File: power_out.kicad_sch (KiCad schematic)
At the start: 20 parts, among them Q501 BTN8962TA, Q502 BTN8962TA, U501 BTT6200-4ESA

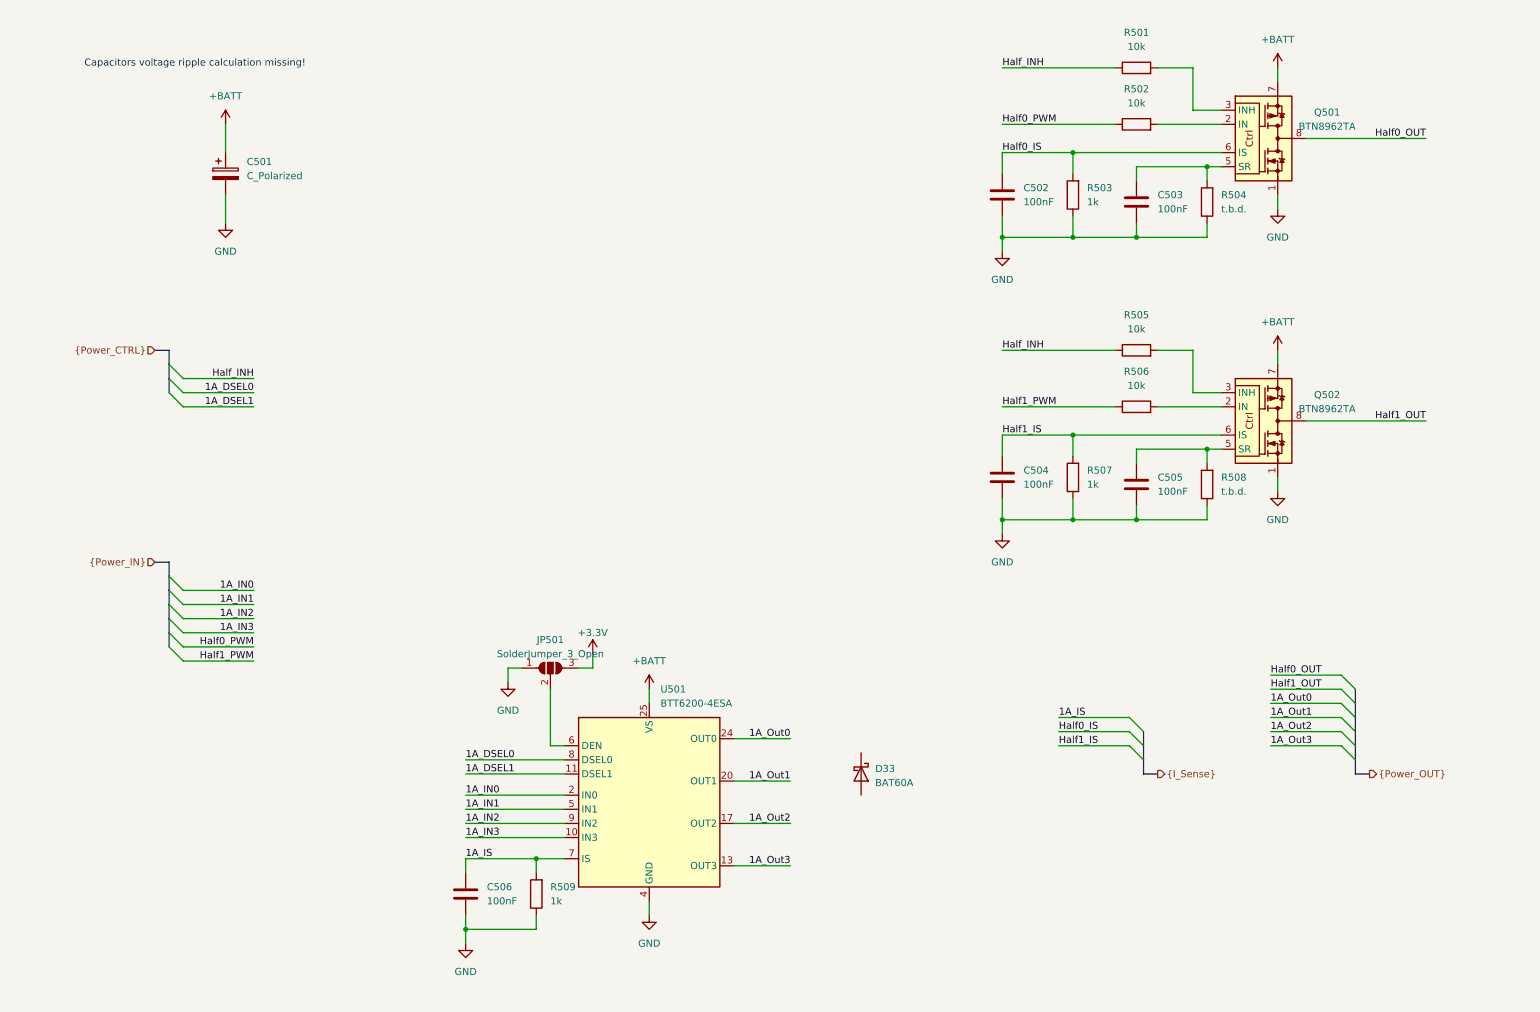
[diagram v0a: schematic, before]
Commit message: added net-classes
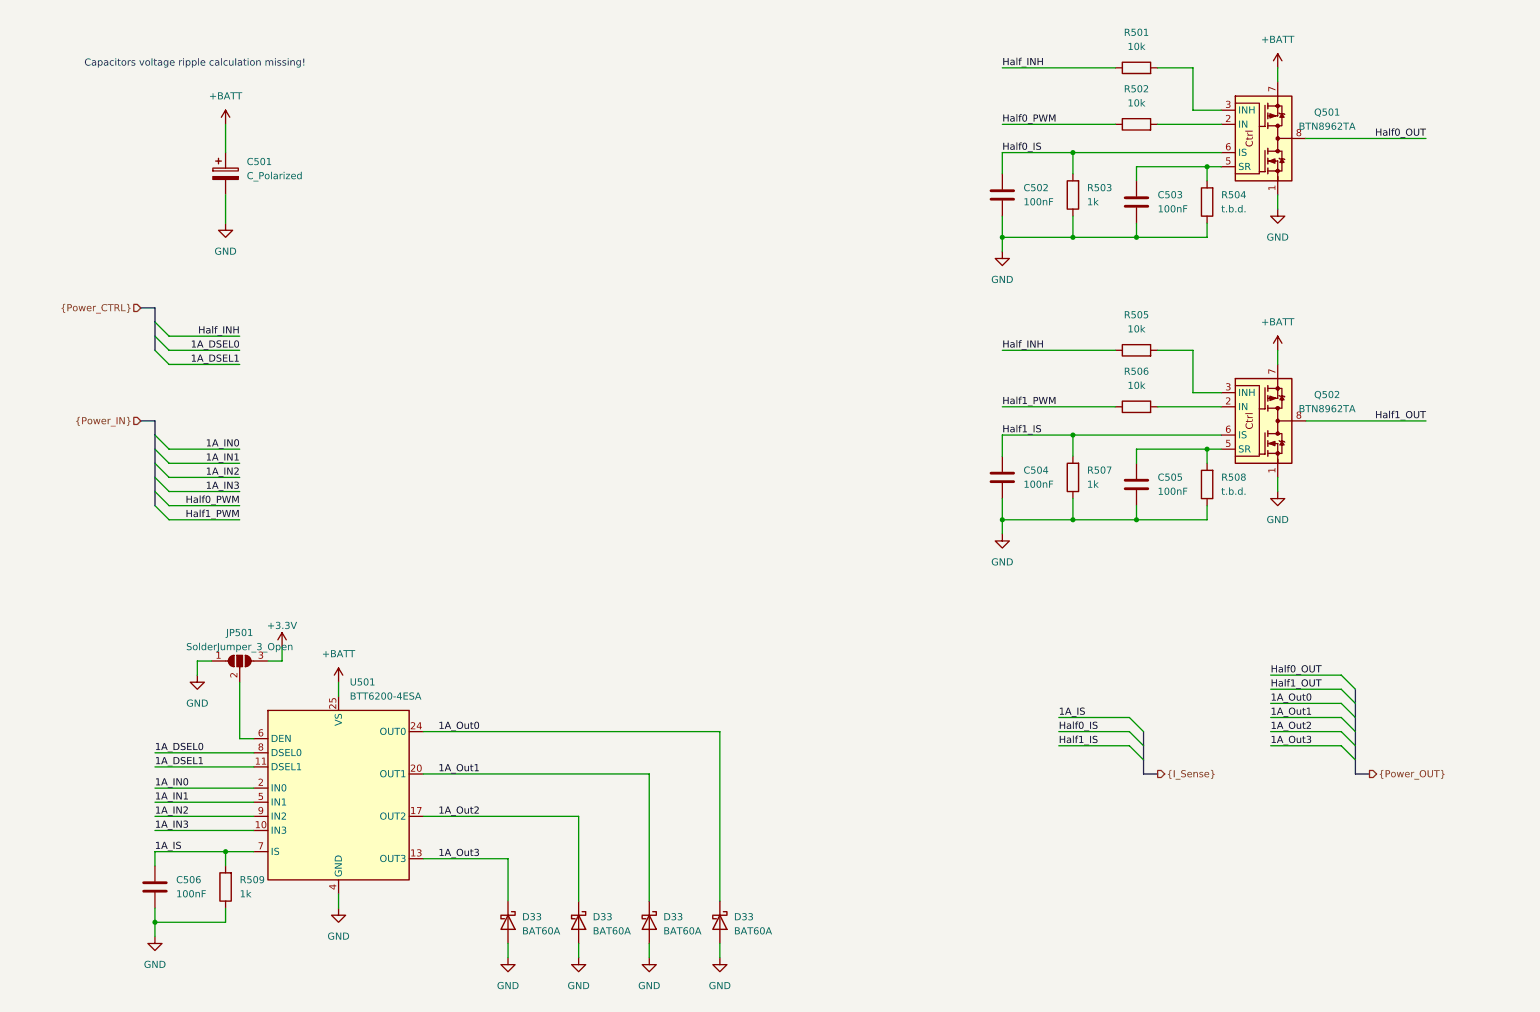
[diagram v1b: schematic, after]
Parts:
- added D33 (x3): BAT60A, Diode_SMD:D_SOD-323, symbol Diode:BAT60A
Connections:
- net 1A_Out0: now also D33.1 (K)
- net 1A_Out1: now also D33.1 (K)
- net 1A_Out2: now also D33.1 (K)
- net 1A_Out3: now also D33.1 (K)
- net GND: now also D33.2 (A), D33.2 (A), D33.2 (A), D33.2 (A)
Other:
- moved on the sheet: C506, D33, JP501, R509, U501

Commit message: completed schematic
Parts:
- removed D33 (x4): BAT60A, Diode_SMD:D_SOD-323, symbol Diode:BAT60A
- added C507: 220µ, symbol Device:C_Polarized
- added C508, C509, C510, C511, C512, C513, C518: 100nF, Capacitor_SMD:C_0603_1608Metric, symbol Device:C
- added C514, C515, C516, C517: 10n, Capacitor_SMD:C_0603_1608Metric, symbol Device:C
- added C519: 1µ, Capacitor_SMD:C_0603_1608Metric, symbol Device:C
- added D501, D502, D503, D504, D513: PMEG4010CEH, Diode_SMD:D_SOD-123F, symbol Diode:PMEG4010CEH
- added D506, D507, D508, D509, D510, D511: BLUE, LED_SMD:LED_0603_1608Metric, symbol Device:LED
- added D512: RED, LED_SMD:LED_0603_1608Metric, symbol Device:LED
- added R510, R511, R512, R513: 100k, Resistor_SMD:R_0603_1608Metric, symbol Device:R
- added R514, R515, R516, R517, R518, R519, R520, R522, R523, R524, R525, R526, R527: 10k, Resistor_SMD:R_0603_1608Metric, symbol Device:R
- added R521: 27, Resistor_SMD:R_0603_1608Metric, symbol Device:R
- added R528: 1k, Resistor_SMD:R_0603_1608Metric, symbol Device:R
- C501: value C_Polarized -> 220µ
- C502, C504: value 100nF -> 1n
- C506: value 100nF -> 100p
- R509: value 1k -> 1.2k
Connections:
- net +3.3V: now also R528.2
- net +BATT: now also C507.1, C509.1, C510.1, C511.1, C513.1, C518.1, C519.1
- net 1A_DSEL0: now also R514.1; no longer U501.8 (DSEL0)
- net 1A_DSEL1: now also R515.1; no longer U501.11 (DSEL1)
- net 1A_IN0: now also R516.1; no longer U501.2 (IN0)
- net 1A_IN1: now also R517.1; no longer U501.5 (IN1)
- net 1A_IN2: now also R518.1; no longer U501.9 (IN2)
- net 1A_IN3: now also R519.1; no longer U501.10 (IN3)
- net 1A_IS: now also R520.2; no longer R509.2, U501.7 (IS)
- net 1A_Out0: now also C517.1, D513.1 (K), R513.2, R524.2
- net 1A_Out1: now also C516.1, D504.1 (K), R512.2, R525.2
- net 1A_Out2: now also C515.1, D503.1 (K), R511.2, R526.2
- net 1A_Out3: now also C514.1, D502.1 (K), R510.2, R527.2
- net GND: now also C507.2, C508.2, C510.2, C512.2, C513.2, C514.2, C515.2, C516.2, C517.2, C518.2, C519.2, D501.1 (K), D502.2 (A), D503.2 (A), D504.2 (A), D506.1 (K), D507.1 (K), D508.1 (K), D509.1 (K), D510.1 (K), D511.1 (K), D513.2 (A), R510.1, R511.1, R512.1, R513.1; no longer U501.4 (GND)
- net Half0_OUT: now also C508.1, C509.2, R523.2
- net Half1_OUT: now also C511.2, C512.1, R522.2
- net Half_INH: now also D512.1 (K)
- new net: R519.2, U501.10 (IN3)
- new net: D508.2 (A), R524.1
- new net: D512.2 (A), R528.1
- new net: D507.2 (A), R522.1
- new net: R517.2, U501.5 (IN1)
- new net: D509.2 (A), R525.1
- new net: R509.2, R520.1, U501.7 (IS)
- new net: D511.2 (A), R527.1
- new net: D501.2 (A), R521.1
- new net: R521.2, U501.4 (GND)
- new net: R514.2, U501.8 (DSEL0)
- new net: D510.2 (A), R526.1
- new net: R516.2, U501.2 (IN0)
- new net: D506.2 (A), R523.1
- new net: R515.2, U501.11 (DSEL1)
- new net: R518.2, U501.9 (IN2)
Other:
- note removed: "Capacitors voltage ripple calculation missing!"
- moved on the sheet: C501, C502, C503, C504, C505, C506, JP501, Q501, Q502, R501, R502, R503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

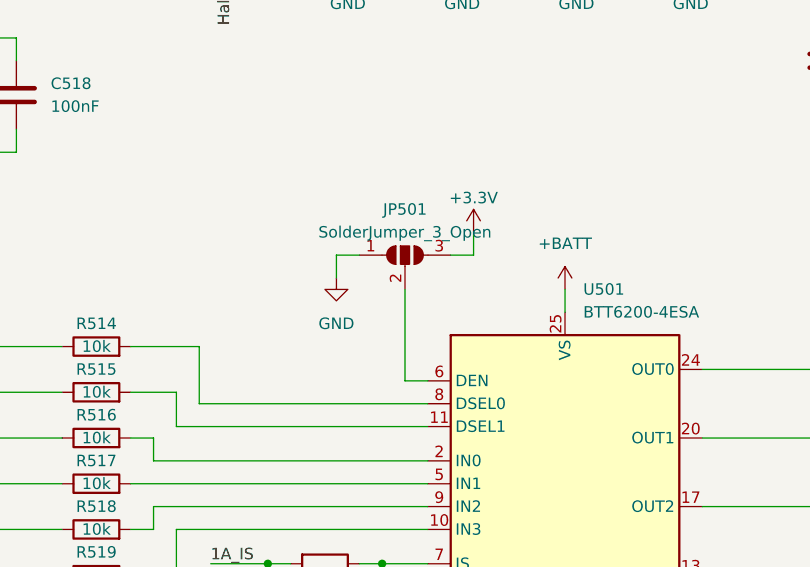
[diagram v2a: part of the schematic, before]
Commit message: placed components and began routing
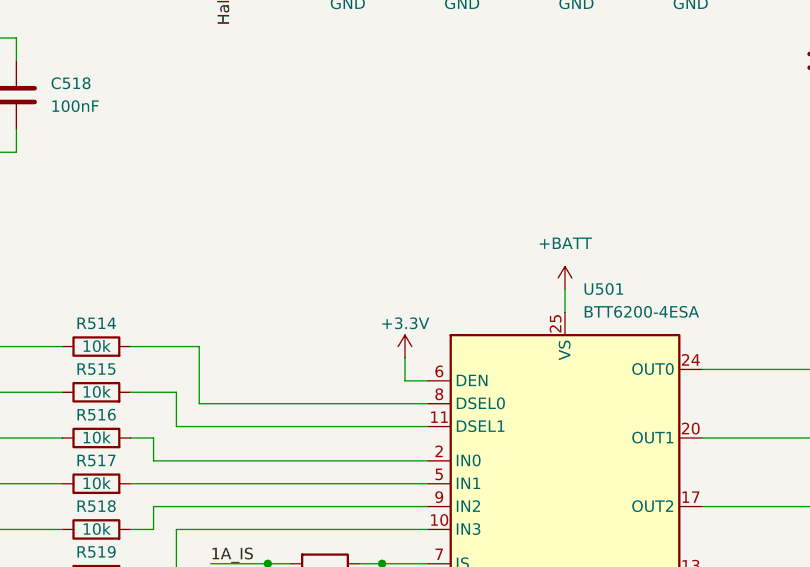
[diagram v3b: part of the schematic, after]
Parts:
- removed JP501: SolderJumper_3_Open, Jumper:SolderJumper-3_P1.3mm_Open_Pad1.0x1.5mm, symbol Jumper:SolderJumper_3_Open
- C501, C507: footprint (none) -> Capacitor_SMD:CP_Elec_10x10.5
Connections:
- net +3.3V: now also U501.6 (DEN)
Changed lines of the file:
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@@
-    (stroke (width 0) (type default))
-  )
-  (wire (pts (xy 74.93 119.38) (xy 72.39 119.38))
     (stroke (width 0) (type default))
   )
@@
     (stroke (width 0) (type default))
   )
-  (wire (pts (xy 87.63 119.38) (xy 87.63 116.84))
-    (stroke (width 0) (type default))
-  )
   (wire (pts (xy 25.4 139.7) (xy 41.91 139.7))
     (stroke (width 0) (type default))
@@
     (stroke (width 0) (type default))
   )
-  (wire (pts (xy 85.09 119.38) (xy 87.63 119.38))
-    (stroke (width 0) (type default))
-  )
   (wire (pts (xy 231.14 57.15) (xy 231.14 59.69))
     (stroke (width 0) (type default))
@@
     (stroke (width 0) (type default))
   )
+  (wire (pts (xy 80.01 130.81) (xy 80.01 133.35))
+    (stroke (width 0) (type default))
+  )
   (wire (pts (xy 190.5 36.83) (xy 231.14 36.83))
     (stroke (width 0) (type default))
@@
     (stroke (width 0) (type default))
   )
-  (wire (pts (xy 80.01 123.19) (xy 80.01 133.35))
-    (stroke (width 0) (type default))
-  )
   (wire (pts (xy 111.76 83.82) (xy 111.76 86.36))
     (stroke (width 0) (type default))
@@
   )
   (wire (pts (xy 113.03 154.94) (xy 118.11 154.94))
-    (stroke (width 0) (type default))
-  )
-  (wire (pts (xy 72.39 119.38) (xy 72.39 121.92))
     (stroke (width 0) (type default))
   )
@@
         (path "/e63e39d7-6ac0-4ffd-8aa3-1841a4541b55/39fda93f-20d1-454a-b043-914b0964bf2d"
           (reference "#PWR0120") (unit 1)
-        )
-      )
-    )
-  )
-  (symbol (lib_id "power:GND") (at 72.39 121.92 0) (unit 1)
-    (in_bom yes) (on_board yes) (dnp no) (fields_autoplaced)
-    (property "Reference" "#PWR0510" (at 72.39 128.27 0)
-      (effects (font (size 1.27 1.27)) hide)
-    )
-    (property "Value" "GND" (at 72.39 127 0)
-      (effects (font (size 1.27 1.27)))
-    )
-    (property "Footprint" "" (at 72.39 121.92 0)
-      (effects (font (size 1.27 1.27)) hide)
-    )
-    (property "Datasheet" "" (at 72.39 121.92 0)
-      (effects (font (size 1.27 1.27)) hide)
-    )
-    (pin "1")
-    (instances
-      (project "Sensor_Board"
-        (path "/e2a0eb17-0eae-4cdd-befd-118f8728b921/c1280e85-b203-4b6b-82d8-dbf0409d7c4d"
-          (reference "#PWR0510") (unit 1)
-        )
-      )
-      (project "FT22_VCU_Konzept"
-        (path "/e63e39d7-6ac0-4ffd-8aa3-1841a4541b55/39fda93f-20d1-454a-b043-914b0964bf2d"
-          (reference "#PWR0126") (unit 1)
         )
       )
@@
     )
   )
-  (symbol (lib_id "power:+3.3V") (at 87.63 116.84 0) (unit 1)
-    (in_bom yes) (on_board yes) (dnp no) (fields_autoplaced)
-    (property "Reference" "#PWR0509" (at 87.63 120.65 0)
-      (effects (font (size 1.27 1.27)) hide)
-    )
-    (property "Value" "+3.3V" (at 87.63 113.03 0)
-      (effects (font (size 1.27 1.27)))
-    )
-    (property "Footprint" "" (at 87.63 116.84 0)
-      (effects (font (size 1.27 1.27)) hide)
-    )
-    (property "Datasheet" "" (at 87.63 116.84 0)
+  (symbol (lib_id "power:+3.3V") (at 80.01 130.81 0) (unit 1)
+    (in_bom yes) (on_board yes) (dnp no) (fields_autoplaced)
+    (property "Reference" "#PWR0509" (at 80.01 134.62 0)
+      (effects (font (size 1.27 1.27)) hide)
+    )
+    (property "Value" "+3.3V" (at 80.01 127 0)
+      (effects (font (size 1.27 1.27)))
+    )
+    (property "Footprint" "" (at 80.01 130.81 0)
+      (effects (font (size 1.27 1.27)) hide)
+    )
+    (property "Datasheet" "" (at 80.01 130.81 0)
       (effects (font (size 1.27 1.27)) hide)
     )
@@
         (path "/e63e39d7-6ac0-4ffd-8aa3-1841a4541b55/39fda93f-20d1-454a-b043-914b0964bf2d"
           (reference "C50") (unit 1)
-        )
-      )
-    )
-  )
-  (symbol (lib_id "Jumper:SolderJumper_3_Open") (at 80.01 119.38 0) (unit 1)
-    (in_bom yes) (on_board yes) (dnp no) (fields_autoplaced)
-    (property "Reference" "JP501" (at 80.01 114.3 0)
-      (effects (font (size 1.27 1.27)))
-    )
-    (property "Value" "SolderJumper_3_Open" (at 80.01 116.84 0)
-      (effects (font (size 1.27 1.27)))
-    )
-    (property "Footprint" "Jumper:SolderJumper-3_P1.3mm_Open_Pad1.0x1.5mm" (at 80.01 119.38 0)
-      (effects (font (size 1.27 1.27)) hide)
-    )
-    (property "Datasheet" "~" (at 80.01 119.38 0)
-      (effects (font (size 1.27 1.27)) hide)
-    )
-    (pin "1")
-    (pin "2")
-    (pin "3")
-    (instances
-      (project "Sensor_Board"
-        (path "/e2a0eb17-0eae-4cdd-befd-118f8728b921/c1280e85-b203-4b6b-82d8-dbf0409d7c4d"
-          (reference "JP501") (unit 1)
         )
       )
@@
       (effects (font (size 1.27 1.27)) (justify left))
     )
-    (property "Footprint" "" (at 220.6752 97.79 0)
+    (property "Footprint" "Capacitor_SMD:CP_Elec_10x10.5" (at 220.6752 97.79 0)
       (effects (font (size 1.27 1.27)) hide)
     )
@@
       (effects (font (size 1.27 1.27)) (justify left))
     )
-    (property "Footprint" "" (at 220.6752 46.99 0)
-      (effects (font (size 1.27 1.27)) hide)
-    )
+    (property "Footprint" "Capacitor_SMD:CP_Elec_10x10.5" (at 220.6752 46.99 0)
+      (effects (font (size 1.27 1.27)) hide)
+    )
